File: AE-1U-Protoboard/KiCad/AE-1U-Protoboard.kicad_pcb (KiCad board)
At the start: 4 copper layers, 25 x 100 mm, 336 parts

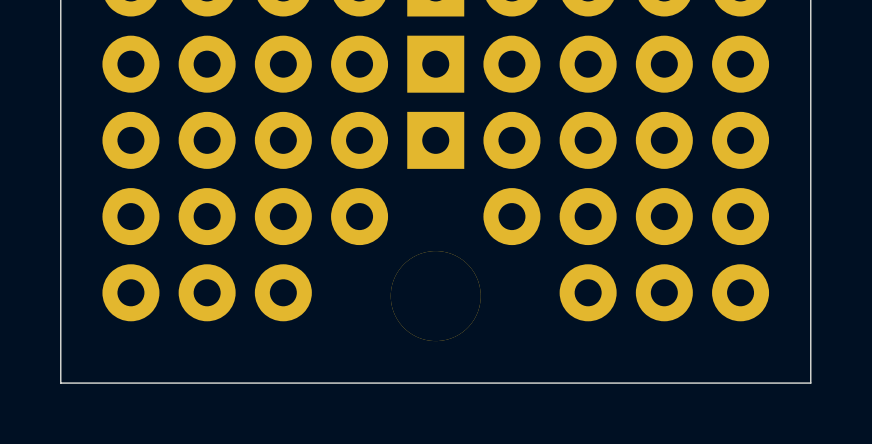
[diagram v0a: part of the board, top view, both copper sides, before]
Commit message: added logo and copyright messages
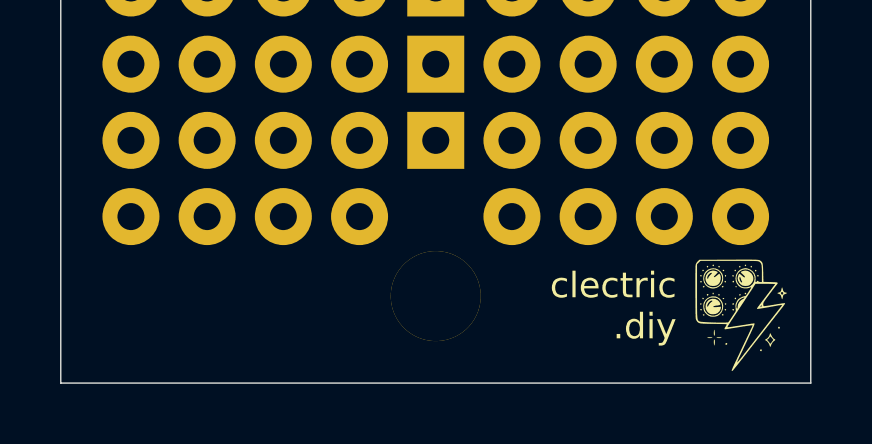
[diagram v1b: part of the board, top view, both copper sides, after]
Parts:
- removed the REF** at (121.5, 149.1)
- removed the REF** at (108.8, 149.1)
- removed the REF** at (111.3, 149.1)
- removed the REF** at (124.0, 149.1)
- removed the REF** at (106.3, 149.1)
- removed the REF** at (126.6, 149.1)
- added G***: LOGO, LOGO, F.Cu at (126.5, 149.9)
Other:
- board text added: "Copyright©2026 clectric.diy"
- board text added: "Licensed under CERN-OHL-W v2"
- board text added: "clectric .diy"
